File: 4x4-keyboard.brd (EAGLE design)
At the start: 76.2 x 76.2 mm, 78 parts, among them J1 M01X1-100MIL-PTH, J10 M01X1-100MIL-PTH, J11 M01X1-100MIL-PTH, J12 M01X1-100MIL-PTH, J13 M01X1-100MIL-PTH, J14 M01X1-100MIL-PTH, J15 M01X1-100MIL-PTH, J16 M01X1-100MIL-PTH, J17 M01X1-100MIL-PTH, J18 M01X1-100MIL-PTH, J19 M01X1-100MIL-PTH, J2 M01X1-100MIL-PTH, J20 M01X1-100MIL-PTH, J21 M01X1-100MIL-PTH, J22 M01X1-100MIL-PTH, J23 M01X1-100MIL-PTH, J24 M01X1-100MIL-PTH, J25 M12-100MIL, J26 M12-100MIL, J3 M01X1-100MIL-PTH, J4 M01X1-100MIL-PTH, J5 M01X1-100MIL-PTH, J6 M01X1-100MIL-PTH, J7 M01X1-100MIL-PTH, J8 M01X1-100MIL-PTH, J9 M01X1-100MIL-PTH

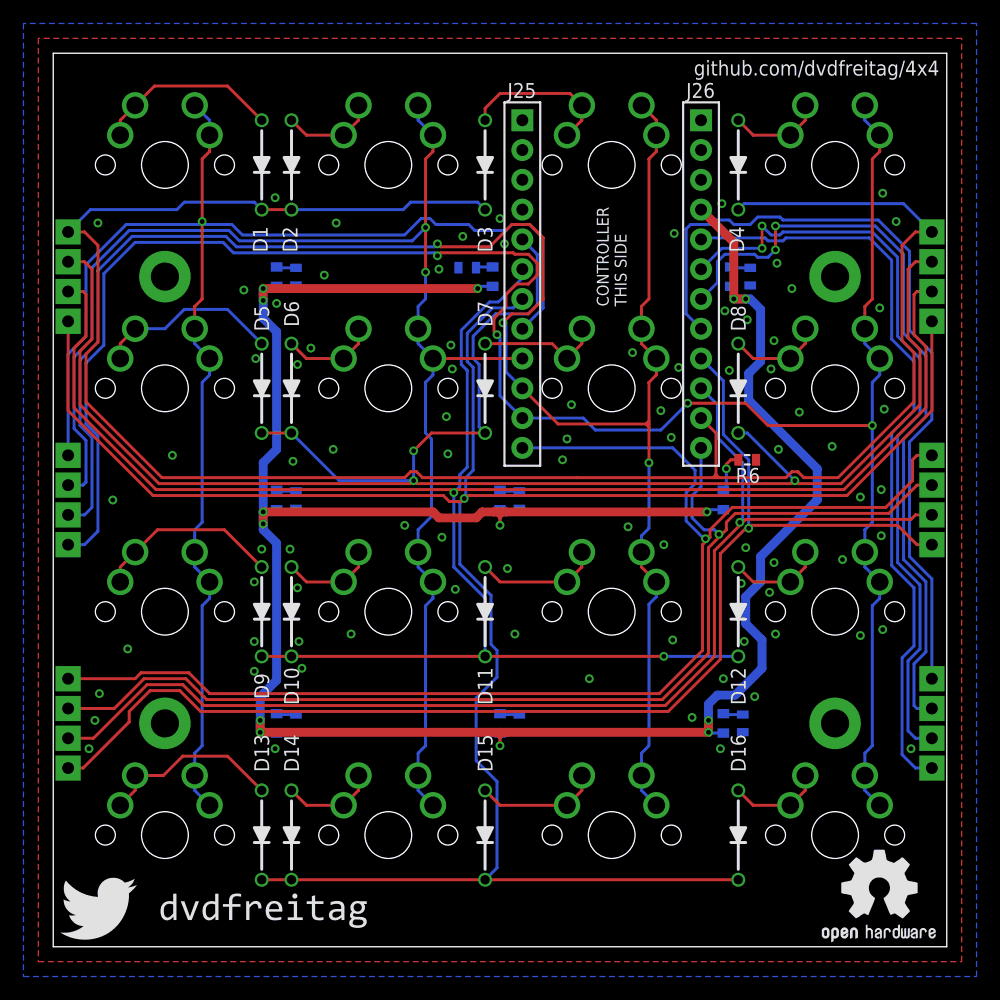
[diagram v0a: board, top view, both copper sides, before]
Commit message: Update layout
- Remove extensible connectors
- Add backlight 3mm leds instead of frontlight smd
- Add I/O-controlled mosfet for driving dimmable backlight
- Add reset switch
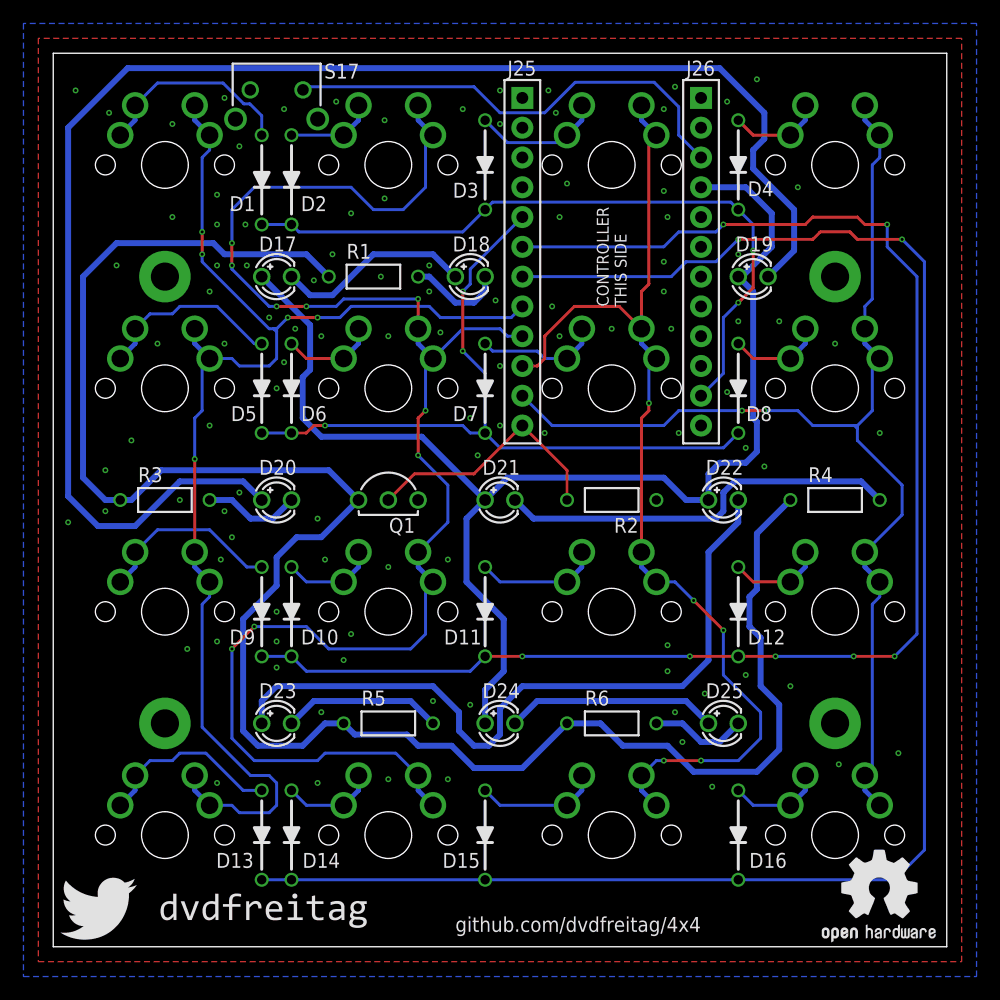
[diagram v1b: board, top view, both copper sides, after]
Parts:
- removed J1, J10, J11, J12, J13, J14, J15, J16, J17, J18, J19, J2, J20, J21, J22, J23, J24, J3, J4, J5, J6, J7, J8, J9: M01X1-100MIL-PTH, Connectors:M01X1_100MIL-PTH
- removed R7, R8, R9: (no value), Passives:0603-CAP
- added Q1: (no value), Passives:TO-92-3
- added S17: TACTILE-PTH-H, Passives:TACTILE-HORIZONTAL
- D17, D18, D19, D20, D21, D22, D23, D24, D25: device Passives:0603-LED -> Passives:3MM-LED
- R1, R3, R4, R5, R6: value (none) -> 56Ω; device Passives:0603-CAP -> Passives:RESISTOR-PTH
- R2: device Passives:0603-CAP -> Passives:RESISTOR-PTH
- moved R3 53.4 mm to (9.53, 38.1), flipped to the top, turned to 0 degrees
- moved R4 46.0 mm to (66.7, 38.1), flipped to the top, turned to 0 degrees
- moved R6 25.3 mm to (47.6, 19.1), turned to 0 degrees
- moved R2 23.3 mm to (47.6, 38.1), flipped to the top
- moved R5 22.1 mm to (28.6, 19.1), flipped to the top, turned to 0 degrees
- moved R1 6.60 mm to (27.3, 57.1), flipped to the top, turned to 0 degrees
- moved D18 1.91 mm to (35.6, 57.1), flipped to the top, turned to 0 degrees
- moved D19 1.91 mm to (59.7, 57.1), flipped to the top, turned to 0 degrees
- moved J25 1.91 mm to (40.0, 72.4)
- moved J26 1.91 mm to (55.2, 72.4)
- moved D1 1.27 mm to (17.8, 65.4)
- moved D2 1.27 mm to (20.3, 65.4)
- flipped D17 to the top, turned to 0 degrees
- flipped D20 to the top, turned to 0 degrees
- flipped D21 to the top, turned to 0 degrees
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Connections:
- removed net COL10: J23.1, J26.6
- removed net COL11: J24.1, J26.5
- removed net COL4: J13.1, J17.1, J25.12
- removed net COL5: J14.1, J18.1, J26.12
- removed net COL6: J15.1, J19.1, J26.10
- removed net COL7: J16.1, J20.1, J26.9
- removed net COL8: J21.1, J26.8
- removed net COL9: J22.1, J26.7
- removed net N$26: D22.C, R6.2
- removed net N$27: D23.C, R7.2
- removed net N$29: D25.C, R9.2
- new net LED: J25.12, Q1.2, R2.P$2
- new net N$34: D19.C, D20.A
- new net N$35: D20.C, R3.P$2
- new net N$36: D18.C, R1.P$2
- new net N$37: D17.C, D18.A
- new net RST: J26.3, S17.1
- net COL0: no longer J9.1
- net COL1: no longer J10.1
- net COL2: no longer J11.1
- net COL3: no longer J12.1
- net GND: now also Q1.1, R2.P$1, S17.2; no longer R1.1, R2.1, R3.1, R4.1, R5.1, R6.1, R7.1, R8.1, R9.1
- net N$22: now also D21.C, R4.P$2; no longer D18.C, R2.2
- net N$23: now also D24.C, D25.A; no longer D19.C, R3.2
- net N$24: now also D22.C, D23.A; no longer D20.C, R4.2
- net N$25: now also D23.C, R5.P$2; no longer D21.C, R5.2
- net N$28: now also D25.C, R6.P$2; no longer D24.C, R8.2
- net N$6: now also Q1.3, R1.P$1, R3.P$1, R4.P$1, R5.P$1, R6.P$1; no longer D17.C, R1.2
- net ROW0: no longer J1.1, J5.1
- net ROW1: no longer J2.1, J6.1
- net ROW2: no longer J3.1, J7.1
- net ROW3: no longer J4.1, J8.1
- net VCC: no longer D18.A, D20.A, D23.A, D25.A
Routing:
- net N$6: track 1.68 -> 168.3 mm
- net N$34: track 0.00 -> 131.0 mm
- net COL4: track 112.3 -> 0.00 mm, vias 1 -> 0
- net ROW0: track 171.8 -> 60.5 mm, vias 0 -> 2
- net COL7: track 106.5 -> 0.00 mm, vias 1 -> 0
- net VCC: track 212.8 -> 111.2 mm, vias 14 -> 0
- net COL6: track 101.5 -> 0.00 mm, vias 1 -> 0
- net COL5: track 98.0 -> 0.00 mm, vias 1 -> 0
- net ROW1: track 157.9 -> 63.5 mm
- net COL3: track 176.7 -> 97.6 mm, vias 4 -> 2
- net COL8: track 68.8 -> 0.00 mm
- net COL2: track 156.5 -> 89.9 mm, vias 3 -> 5
- net COL10: track 66.2 -> 0.00 mm, vias 2 -> 0
- net COL9: track 66.2 -> 0.00 mm, vias 2 -> 0
- net COL11: track 65.3 -> 0.00 mm
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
